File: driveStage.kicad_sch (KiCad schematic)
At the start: 29 parts

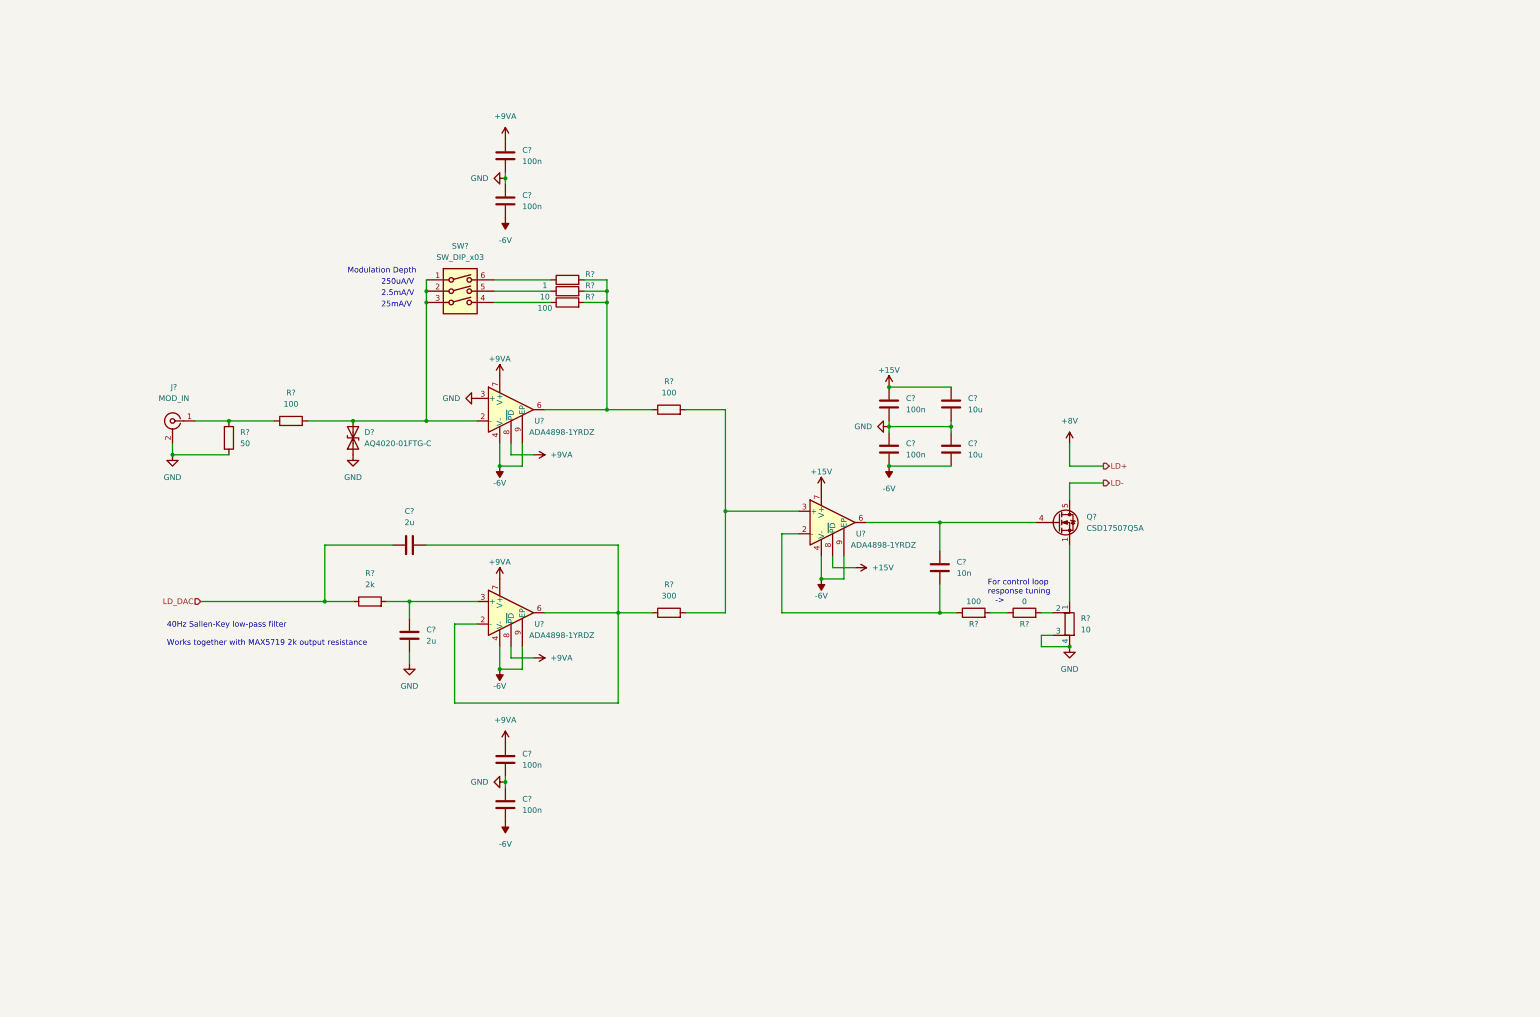
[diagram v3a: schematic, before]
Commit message: remove ref dac sheet, finish thermostat
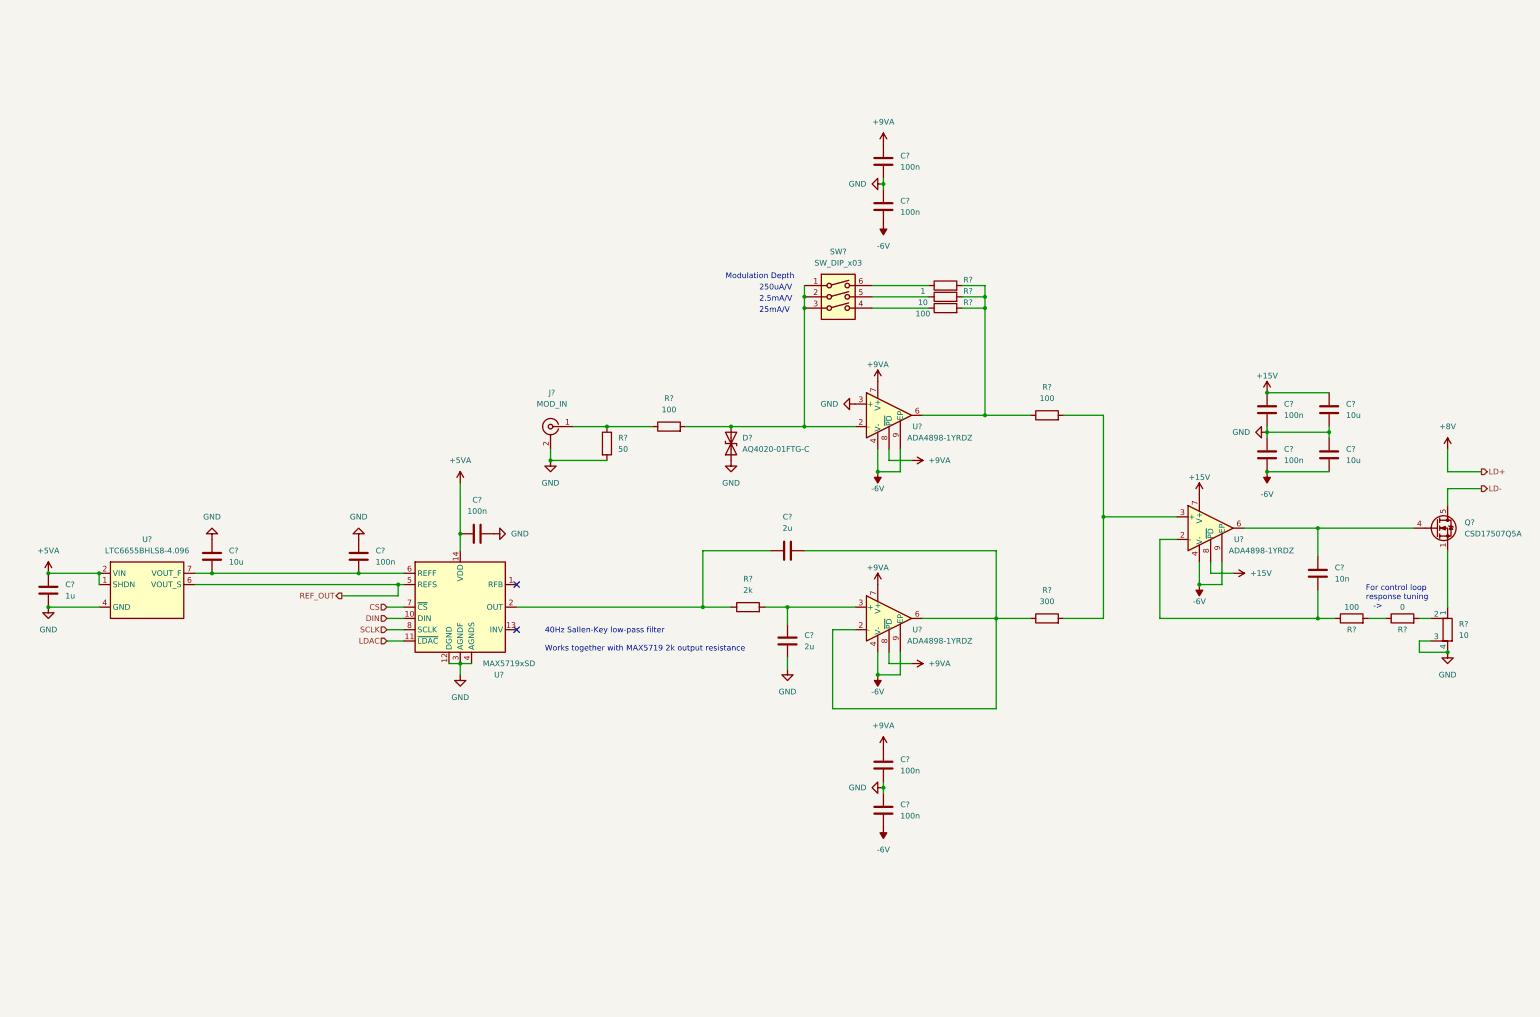
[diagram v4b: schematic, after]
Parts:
- added C?: 10u, symbol Device:C
- added C?: 1u, symbol Device:C
- added C? (x2): 100n, symbol Device:C
- added U?: LTC6655BHLS8-4.096, kirdy:LCC127P500X500X155-8N, symbol kirdy:LTC6655
- added U?: MAX5719xSD, Package_SO:SOIC-14_3.9x8.7mm_P1.27mm, symbol Analog_DAC:MAX5719xSD
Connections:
- net GND: now also C?.1, C?.1, C?.2, C?.2, U?.12 (DGND), U?.3 (AGNDF), U?.3 (GND), U?.4 (AGNDS), U?.4 (GND), U?.5 (GND), U?.8 (GND)
- net LD_DAC: no longer names the net of C?.1, R?.1
- net LD_DAC: now also U?.2 (OUT)
- new net: C?.2, C?.2, U?.6 (REFF), U?.7 (VOUT_F)
- new net +5VA: C?.1, C?.1, U?.1 (SHDN), U?.14 (VDD), U?.2 (VIN)
- new net CS: U?.7 (~{CS})
- new net DIN: U?.10 (DIN)
- new net LDAC: U?.11 (~{LDAC})
- new net REF_OUT: U?.5 (REFS), U?.6 (VOUT_S)
- new net SCLK: U?.8 (SCLK)
- no-connect marks 0 -> 2
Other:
- moved on the sheet: C?, D?, J?, Q?, R?, SW?, U?

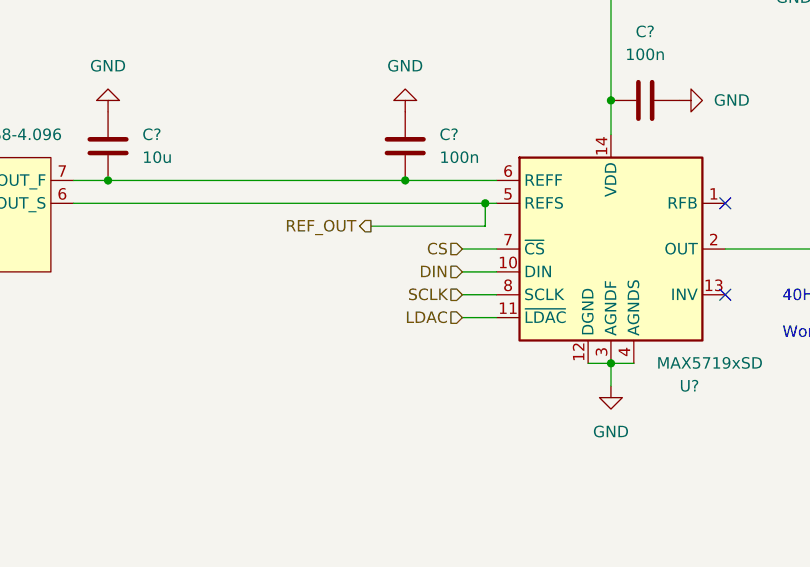
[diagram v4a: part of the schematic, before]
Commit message: add TEC V sense, filter TEC I sense
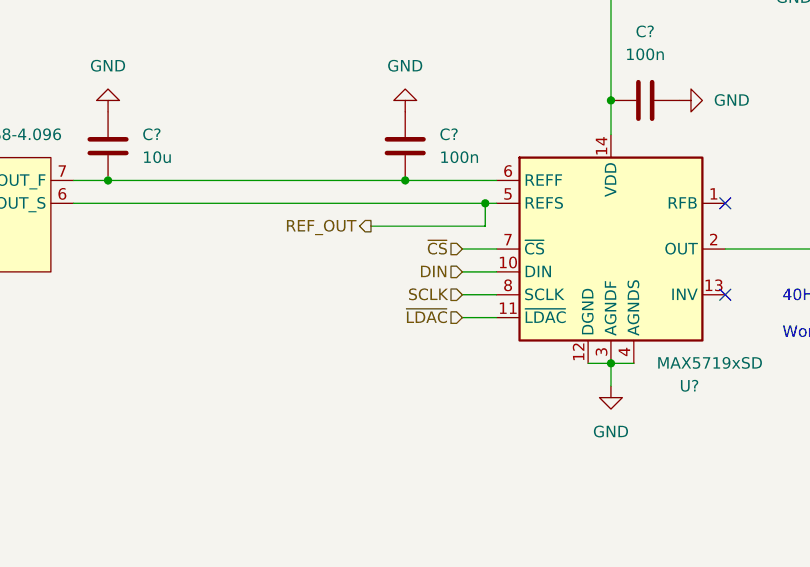
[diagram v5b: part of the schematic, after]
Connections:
- net CS renamed ~{CS}
- net LDAC renamed ~{LDAC}
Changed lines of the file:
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@@
     (effects (font (size 1.27 1.27)) (justify left bottom))
   )
-  (hierarchical_label "LDAC" (shape input) (at 135.89 162.56 180)
+  (hierarchical_label "~{LDAC}" (shape input) (at 135.89 162.56 180)
     (effects (font (size 1.27 1.27)) (justify right))
   )
@@
     (effects (font (size 1.27 1.27)) (justify left))
   )
-  (hierarchical_label "CS" (shape input) (at 135.89 154.94 180)
+  (hierarchical_label "~{CS}" (shape input) (at 135.89 154.94 180)
     (effects (font (size 1.27 1.27)) (justify right))
   )

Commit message: polish
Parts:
- added J? (x2): DNP, symbol Connector:Conn_Coaxial
- C?: value 1u -> 2u
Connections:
- net GND: now also J?.2 (Ext), J?.2 (Ext); no longer R?.3
- net at R?.2, R?.2: now also J?.1 (In)
- new net: J?.1 (In), R?.3
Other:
- note added: "All capacitors PPS film type to prevent microphonics"
- note added: "For control loop response tuning"
- note added: "For noise measurement"
- note removed: "40Hz Sallen-Key low-pass filter Works together with MAX5719 2k output resistance"
- note removed: "For control loop response tuning ->"
- moved on the sheet: C?, R?

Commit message: before beer
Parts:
- removed C? (x4): 100n, symbol Device:C
- added C? (x5): 100n, symbol Device:C
- added C?: 1.6n, symbol Device:C
- added D?: BAV99, Package_TO_SOT_SMD:SOT-23, symbol Diode:BAV99
- added R? (x2): 1k, symbol Device:R
- added U? (x3): RS8552, Package_SO:SOIC-8_3.9x4.9mm_P1.27mm, symbol kirdy:RS8552
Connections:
- net +9VA: now also C?.1, C?.1
- net -6V: now also C?.2, C?.2
- net GND: now also J?.1 (In), R?.3, C?.1, C?.1, C?.1, C?.2, C?.2, D?.1 (K), U?.4 (V-), U?.5 (+), U?.6 (-)
- new net: C?.2, R?.1, U?.3 (+)
- new net +3.3VA: D?.2 (A), U?.8 (V+)
- new net PD_BIAS: R?.2
- new net PD_C: C?.2, D?.3 (K), R?.2, U?.2 (-)
- new net PD_MON: C?.1, R?.1, U?.1
- no-connect marks 2 -> 3
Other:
- moved on the sheet: C?, D?, J?, Q?, R?, SW?, U?

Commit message: add PoE
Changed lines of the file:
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@@
       (effects (font (size 1.27 1.27)) hide)
     )
-    (pin "1")
-    (pin "2")
-    (pin "3")
     (pin "5")
     (pin "6")
     (pin "7")
-    (pin "4")
-    (pin "8")
   )
   (symbol (lib_id "kirdy:RS8552") (at 339.09 208.28 0) (mirror y) (unit 1)
@@
     (pin "2")
     (pin "3")
-    (pin "5")
-    (pin "6")
-    (pin "7")
-    (pin "4")
-    (pin "8")
   )
   (symbol (lib_id "power:GND") (at 96.52 99.06 180) (unit 1)
@@
       (effects (font (size 1.27 1.27)) hide)
     )
-    (pin "1")
-    (pin "2")
-    (pin "3")
-    (pin "5")
-    (pin "6")
-    (pin "7")
     (pin "4")
     (pin "8")
